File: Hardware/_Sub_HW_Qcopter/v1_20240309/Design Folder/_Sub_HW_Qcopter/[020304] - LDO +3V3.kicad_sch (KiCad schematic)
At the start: 6 parts, among them U3501 TLV74033PDBVR

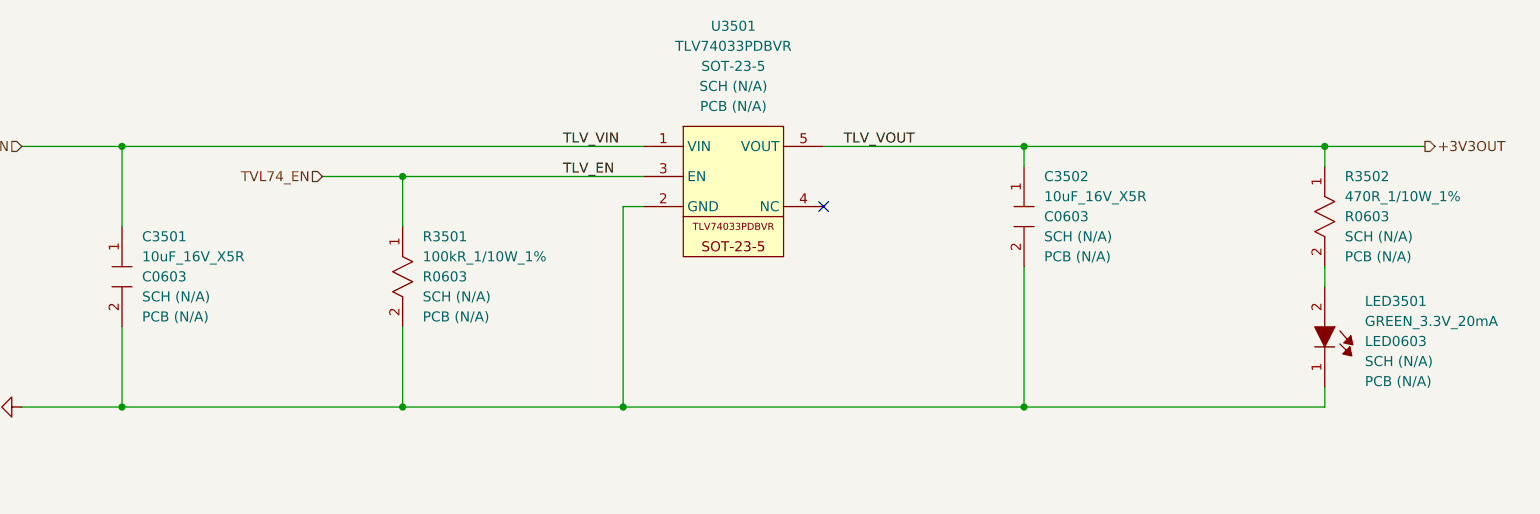
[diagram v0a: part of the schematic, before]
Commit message: Update [020304] - LDO +3V3.kicad_sch
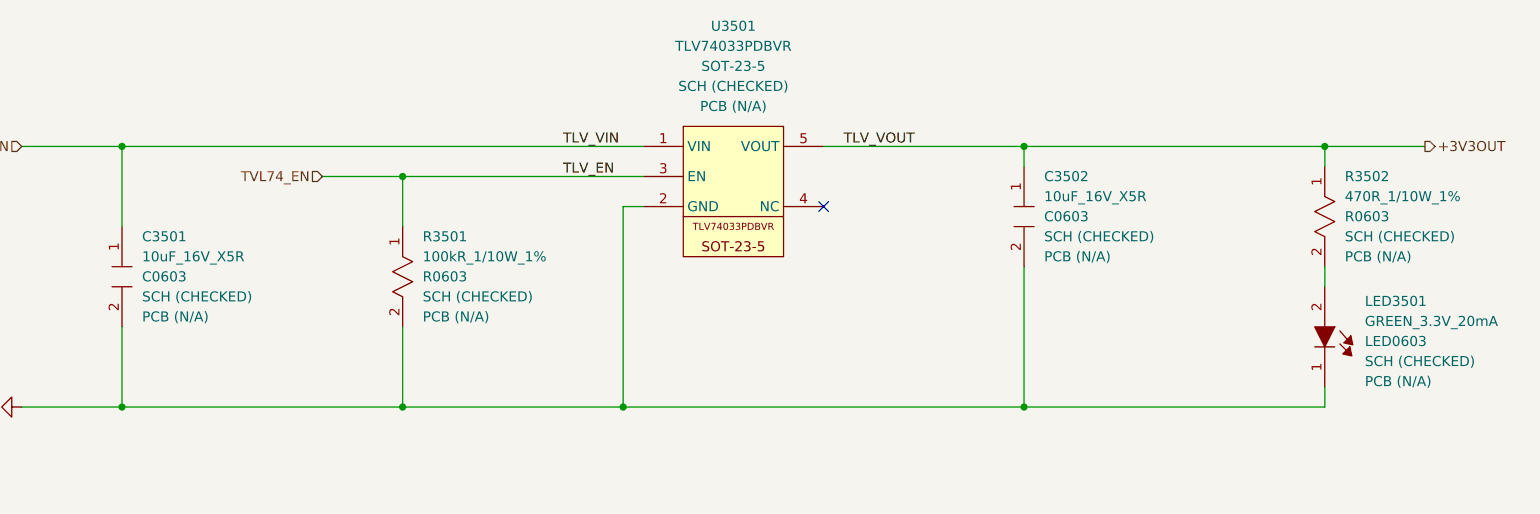
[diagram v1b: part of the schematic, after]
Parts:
- C3501, C3502, LED3501, R3501, R3502, U3501: SCH CHECK SCH (N/A) -> SCH (CHECKED)
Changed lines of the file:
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@@
 			)
 		)
-		(property "SCH CHECK" "SCH (N/A)"
+		(property "SCH CHECK" "SCH (CHECKED)"
 			(at 215.9 212.0899 90)
 			(effects
@@
 			)
 		)
-		(property "SCH CHECK" "SCH (N/A)"
+		(property "SCH CHECK" "SCH (CHECKED)"
 			(at 294.64 204.4699 90)
 			(effects
@@
 			)
 		)
-		(property "SCH CHECK" "SCH (N/A)"
+		(property "SCH CHECK" "SCH (CHECKED)"
 			(at 335.28 220.2814 90)
 			(effects
@@
 			)
 		)
-		(property "SCH CHECK" "SCH (N/A)"
+		(property "SCH CHECK" "SCH (CHECKED)"
 			(at 255.27 185.42 0)
 			(effects
@@
 			)
 		)
-		(property "SCH CHECK" "SCH (N/A)"
+		(property "SCH CHECK" "SCH (CHECKED)"
 			(at 180.34 212.0899 90)
 			(effects
@@
 			)
 		)
-		(property "SCH CHECK" "SCH (N/A)"
+		(property "SCH CHECK" "SCH (CHECKED)"
 			(at 332.74 204.4699 90)
 			(effects
